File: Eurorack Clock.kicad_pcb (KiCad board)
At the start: 2 copper layers, 156.5 x 128.5 mm, 80 parts, among them J1 Conn_01x10_Pin, J10 CLK/16, J10X CLK/16, J11 Conn_02x08_Row_Letter_Last, J12 Conn_01x02_Pin, J13 Conn_01x02_Socket, J2 Conn_01x08_Pin, J3 Clock In, J3X Clock In, J4 Conn_01x10_Socket, J5 Conn_01x08_Pin, J6 CLK, J6X CLK, J7 CLK/2, J7X CLK/2, J8 CLK/4, J8X CLK/4, J9 CLK/8, J9X CLK/8, SW1 RotaryEncoder_DualWithSwitch, SW1X RotaryEncoder_DualWithSwitch, SW2 Run/Stop, SW2X Run/Stop, SW3 Reset, SW3X Reset, U1 ULN2003, U6 L7805

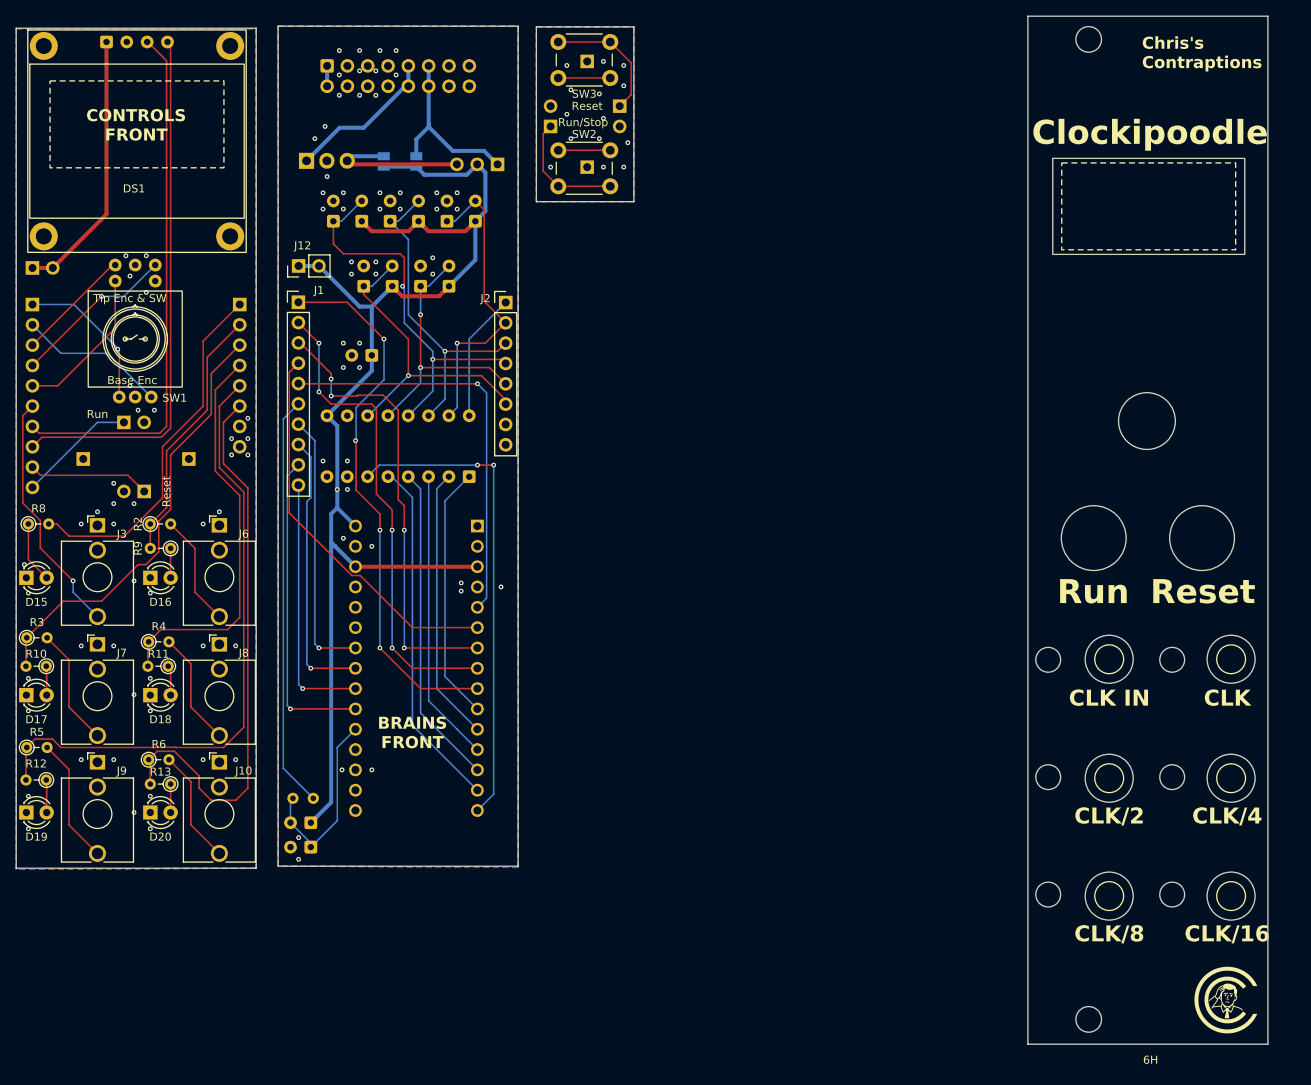
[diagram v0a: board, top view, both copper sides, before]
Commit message: Relabeled outputs on schematic and panel, cleaned up pcb layout, removed unused headers, added logo - still need to add to panel
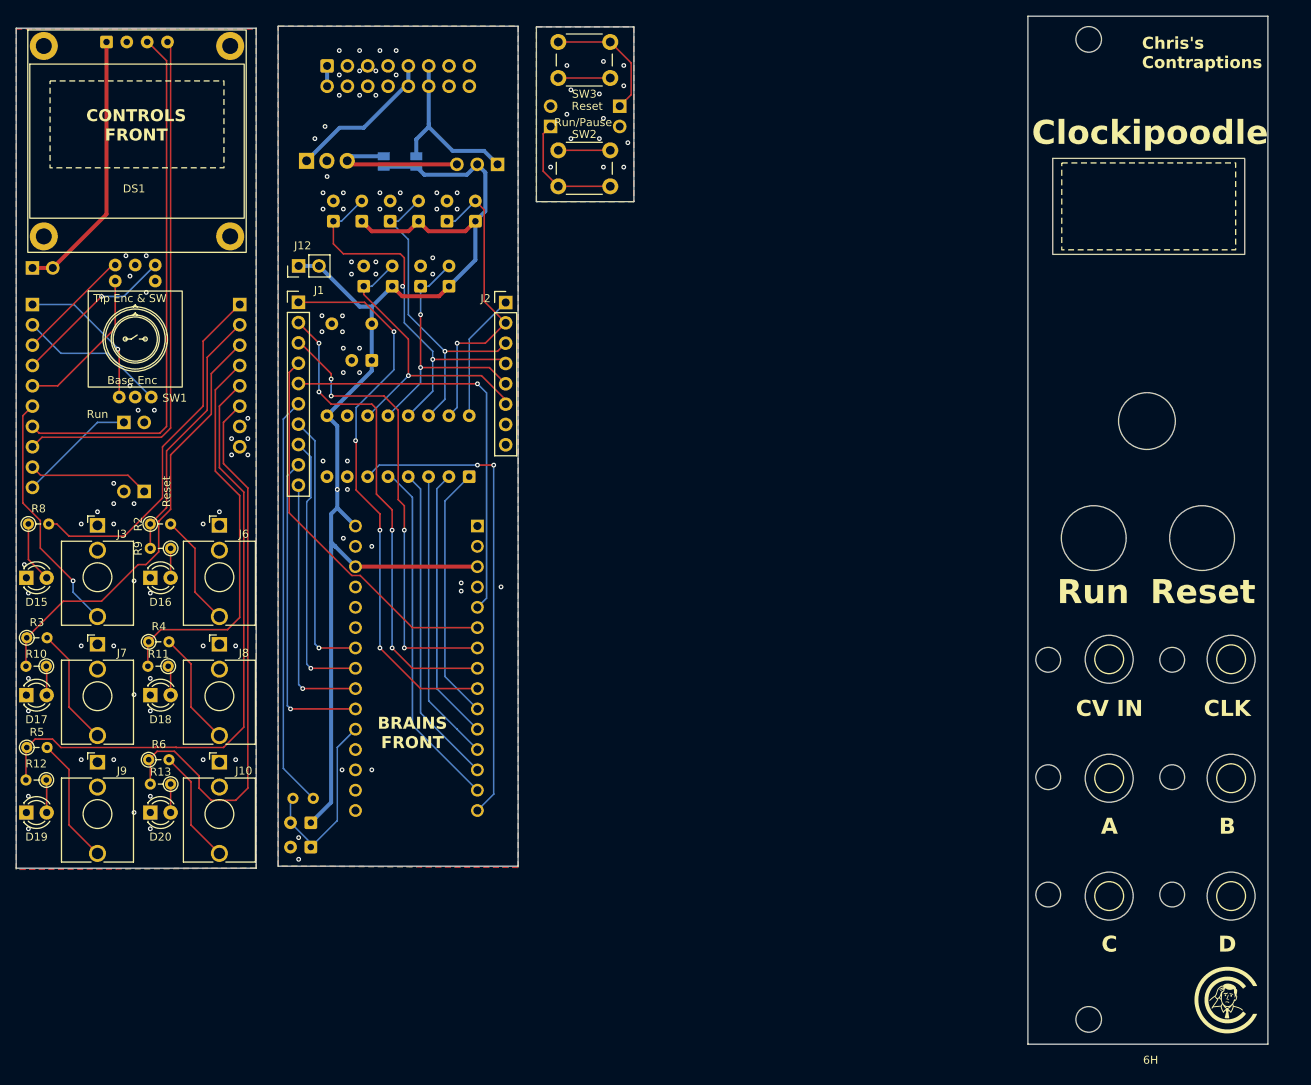
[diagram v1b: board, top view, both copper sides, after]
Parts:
- removed REF_Stand1, REF_Stand1A, REF_Stand2, REF_Stand2A: PinHeader_1x01_P2.54mm_Vertical, Connector_PinHeader_2.54mm:PinHeader_1x01_P2.54mm_Vertical
- added C3: 100n, Capacitor_THT:C_Disc_D4.7mm_W2.5mm_P5.00mm, B.Cu at (62.2, 78.0)
- C1: value 0.1u -> 10u; footprint Capacitor_THT:CP_Radial_D10.0mm_P2.50mm -> Capacitor_THT:CP_Radial_D5.0mm_P2.50mm
- J10: value CLK/16 -> CLK/D
- J3: value Clock In -> CV In
- J3X: value Clock In -> CV IN
- J7: value CLK/2 -> CLK/A
- J8: value CLK/4 -> CLK/B
- J9: value CLK/8 -> CLK/C
- SW2: value Run/Stop -> Run/Pause
- moved C1 0.63 mm to (62.2, 82.6)
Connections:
- net CLK_IN renamed CV_IN
- net CLK_IN_LED renamed CV_IN_LED
- net CLK/16 renamed CLK/D
- net CLK/2 renamed CLK/A
- net CLK/4 renamed CLK/B
- net CLK/8 renamed CLK/C
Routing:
- net A: track 87.3 -> 89.6 mm
- net +5V: track 194.6 -> 195.2 mm
- net GND: vias 104 -> 108
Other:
- board text added: "A"
- board text added: "B"
- board text added: "C"
- board text added: "CV IN"
- board text added: "Clockipoodle V0.2 Board 1/3 Christian Cooper Jan 2026"
- board text added: "Clockipoodle V0.2 Board 2/3 Christian Cooper Jan 2026"
- board text added: "Clockipoodle V0.2 Front Panel Christian Cooper Jan 2026"
- board text added: "D"
- board text removed: "CLK IN"
- board text removed: "CLK/16"
- board text removed: "CLK/2"
- board text removed: "CLK/4"
- board text removed: "CLK/8"
- board text removed: "Clockipoodle V0.1 Board 1/3 Christian Cooper Jan 2026"
- board text removed: "Clockipoodle V0.1 Board 2/3 Christian Cooper Jan 2026"
- board text removed: "Clockipoodle V0.1 Front Panel Christian Cooper Jan 2026"
